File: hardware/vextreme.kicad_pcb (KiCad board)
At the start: 2 copper layers, 48 x 66.1 mm, 49 parts, among them CON1 vectrex-edge-connector, J1 USB_C_Receptacle_USB2.0, J2 Conn_01x06_Male, U1 LM1117-3.3, U2 STM32F411RCTx, U3 74HC32, U4 SN74LVC8T245DB, U5 W25Q128, Y1 8MHz

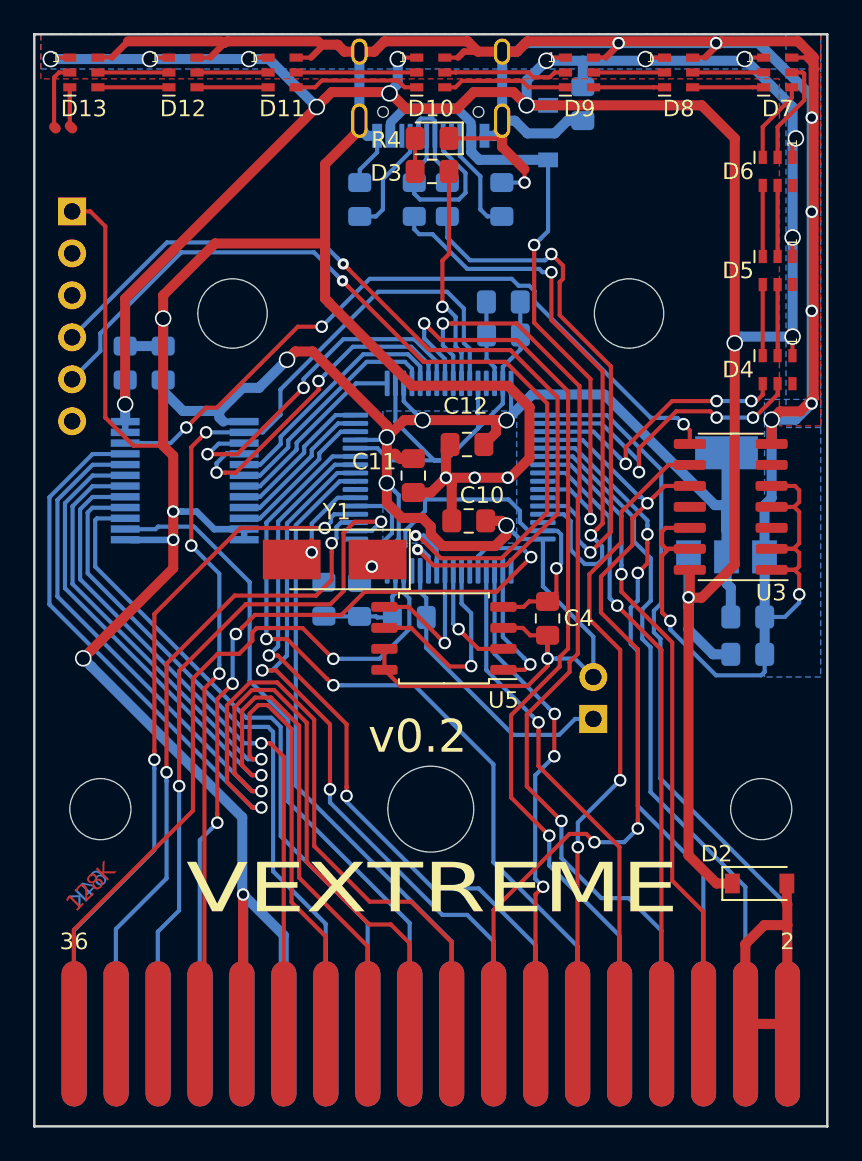
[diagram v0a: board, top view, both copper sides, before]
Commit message: v0.3 Hardware Changes
    - moved vextreme symbol library into libs/ folder
    - renaming 'veccart' to 'vextreme' for hardware files
    - Generate v0.3 gerbers, pdf and BOM
    - Finish routing v0.3 PCB
    - Fixes #21, added VEXTREME logo to PCB
    - Also moved most components to the bottom side and unrouted to prepare for single-sided conversion
    - Fixes #18, Add ESD protection to USB
    - Fixes #36, add test points for power rails.  Also add VEC-5V to PA10 to detect when Vectrex is on/off
    - Fixes #15, replace U3 with a single OR gate and add optional R7 to omit U3 completely
    - add SW1 for programming, add SW2 for STM32 reset
    - adds 3-pin header for LED output
    - Fixes #13, move the debugging/serial port connector so it does not interfere with enclosure bosses
    - Fixes #9, R4 & D3 reference designators are swapped
    - Fixes #12, reduce from 10 to 4 LEDs
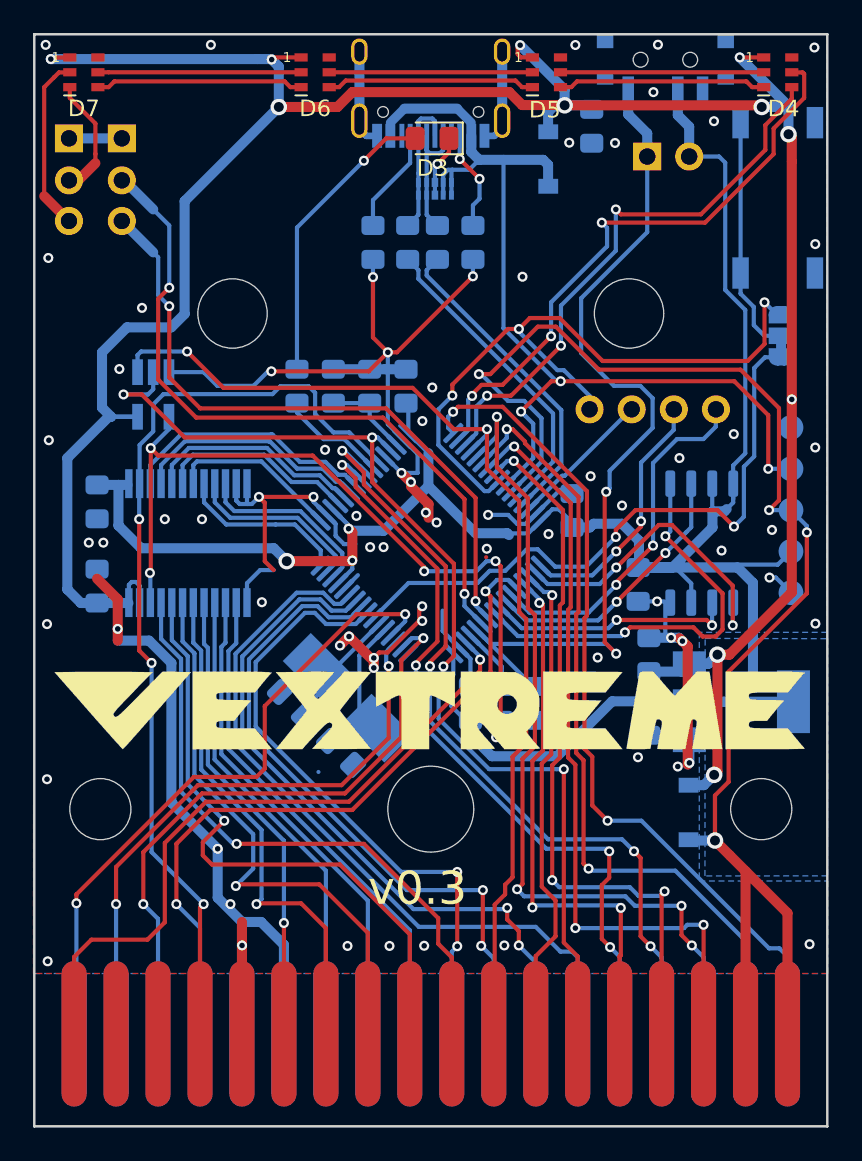
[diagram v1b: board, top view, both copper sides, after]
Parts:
- removed D10, D12, D8: APA102-2020, vextreme:LED-APA102-2020_6_REV_2
- removed the D4 at (162.7, 91.0)
- removed the D5 at (162.7, 85.0)
- removed the D6 at (162.7, 79.0)
- removed REF**: KiCad-Logo2_5mm_SilkScreen, Symbol:KiCad-Logo2_5mm_SilkScreen
- removed REF**: OSHW-Logo2_7.3x6mm_SilkScreen, Symbol:OSHW-Logo2_7.3x6mm_SilkScreen
- added G***: LOGO, vextreme:vextreme-logo, B.Cu at (141.7, 122.8)
- added G***: LOGO, vextreme:vextreme-logo, F.Cu at (141.7, 111.6)
- added J3: Conn_01x03_Male, Connector_PinHeader_2.54mm:PinHeader_1x03_P2.54mm_Vertical, B.Cu at (119.8, 77.0)
- added JP2: Jumper_3_Bridged12, vextreme:SolderJumper-3_P1.3mm_Bridged12_RoundedPad1.0x1.5mm_NumberLabels, B.Cu at (162.9, 89.0)
- added R7: 0, Resistor_SMD:R_0805_2012Metric_Pad1.15x1.40mm_HandSolder, B.Cu at (146.0, 111.2)
- added SP1: PA8, vextreme:SparePin_1x01_P2.54mm_Vertical, B.Cu at (151.3, 93.4)
- added SP2: PA13, vextreme:SparePin_1x01_P2.54mm_Vertical, B.Cu at (153.8, 93.4)
- added SP3: PA14, vextreme:SparePin_1x01_P2.54mm_Vertical, B.Cu at (156.4, 93.4)
- added SP4: PD2, vextreme:SparePin_1x01_P2.54mm_Vertical, B.Cu at (158.9, 93.4)
- added SW1: K3-1296S-E2, vextreme:SW_SPDT_K3-1296S-E2, B.Cu at (155.9, 72.6)
- added SW2: TS-1002S-11526C, vextreme:SW_Push_1P1T_NO_6x6mm_H11.5mm, B.Cu at (162.7, 80.6)
- added TP1: V5V, TestPoint:TestPoint_Pad_D1.5mm, B.Cu at (163.5, 99.5)
- added TP2: 5V, TestPoint:TestPoint_Pad_D1.5mm, B.Cu at (163.5, 94.5)
- added TP3: GND, TestPoint:TestPoint_Pad_D1.5mm, B.Cu at (163.5, 104.5)
- added TP4: U5V, TestPoint:TestPoint_Pad_D1.5mm, B.Cu at (163.5, 97.0)
- added TP5: 3V3, TestPoint:TestPoint_Pad_D1.5mm, B.Cu at (163.5, 102.0)
- added U6: TPD4E02B04DQA, vextreme:USON-10_2.5x1.0mm_P0.5mm_passthrough, B.Cu at (141.9, 80.0)
- C10, C11, C12, C4, D2, R4, U5, Y1: moved to B.Cu
- C13: value 47u -> 10u
- J2: value Conn_01x06_Male -> Conn_01x03_Male; footprint Connector_PinHeader_2.54mm:PinHeader_1x06_P2.54mm_Vertical -> Connector_PinHeader_2.54mm:PinHeader_1x03_P2.54mm_Vertical
- U3: value 74HC32 -> 74LVC1G32; footprint Package_SO:SOIC-14_3.9x8.7mm_P1.27mm -> vextreme:SOT-23-5_HandSoldering; moved to B.Cu
- moved U3 35.6 mm to (124.9, 92.5), turned to 270 degrees
- moved JP1 34.2 mm to (154.8, 78.1), turned to 270 degrees
- moved U5 16.6 mm to (158.1, 101.5), turned to 90 degrees
- moved R4 15.4 mm to (133.6, 92.0), turned to 270 degrees
- moved C5 13.6 mm to (121.5, 104.1)
- moved U1 12.0 mm to (160.5, 111.1), turned to 0 degrees
- moved C6 11.5 mm to (135.8, 92.0), turned to 90 degrees
- moved C10 11.0 mm to (144.1, 111.2), turned to 90 degrees
- moved C11 9.84 mm to (150.2, 99.5), turned to 90 degrees
- moved C8 9.36 mm to (136.3, 114.2), turned to 315 degrees
- moved C3 9.30 mm to (121.5, 99.0), turned to 270 degrees
- moved R3 9.13 mm to (147.9, 111.2), turned to 270 degrees
- moved C7 8.67 mm to (138.0, 92.0), turned to 90 degrees
- moved C2 8.57 mm to (154.9, 112.1), turned to 270 degrees
- moved Y1 8.41 mm to (136.7, 110.9), turned to 135 degrees
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- renumbered D7 to D4, D9 to D5, D11 to D6, D13 to D7
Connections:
- net USB-IN renamed USB-5V
- CON1 pad 2: C_VCC -> VEC-5V
- CON1 pad 4: C_VCC -> VEC-5V
- D2 pad 2: C_VCC -> VEC-5V
- D4 pad 2: Net-(D7-Pad2) (its old number) -> Net-(D4-Pad2)
- D4 pad 3: Net-(D7-Pad3) (its old number) -> Net-(D4-Pad3)
- D4 pad 4: Net-(D6-Pad3) -> SDAT
- D4 pad 5: Net-(D6-Pad2) -> SCLK
- D5 pad 2: Net-(D10-Pad5) -> Net-(D5-Pad2)
- D5 pad 3: Net-(D10-Pad4) -> Net-(D5-Pad3)
- D5 pad 4: SDAT_CONT -> Net-(D4-Pad3)
- D5 pad 5: SCLK_CONT -> Net-(D4-Pad2)
- D6 pad 2: Net-(D11-Pad2) -> Net-(D6-Pad2)
- D6 pad 3: Net-(D11-Pad3) -> Net-(D6-Pad3)
- D6 pad 4: Net-(D10-Pad3) -> Net-(D5-Pad3)
- D6 pad 5: Net-(D10-Pad2) -> Net-(D5-Pad2)
- D7 pad 4: Net-(D12-Pad3) -> Net-(D6-Pad3)
- D7 pad 5: Net-(D12-Pad2) -> Net-(D6-Pad2)
- J2 pad 2: Net-(J2-Pad2) -> RXD
- J2 pad 3: Net-(J2-Pad3) -> TXD
- U2 pad 29: Net-(U2-Pad29) -> V-OE
- U2 pad 41: Net-(U2-Pad41) -> PA8
- U2 pad 43: Net-(U2-Pad43) -> VEC-5V
- U2 pad 7: Net-(U2-Pad7) -> NRST
- U3 pad 1: GND -> V-CE
- U3 pad 2: GND -> V-OE
- U3 pad 3: Net-(U3-Pad3) -> GND
- U3 pad 4: GND -> Net-(R7-Pad1)
- U3 pad 5: GND -> +5V
- U4 pad 22: Net-(U3-Pad8) -> Net-(R7-Pad1)
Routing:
- net GND: track 421.8 -> 175.5 mm, vias 19 -> 74
- net VEC-5V: track 0.00 -> 88.3 mm, vias 0 -> 4
- net Net-(R7-Pad1): track 0.00 -> 48.2 mm, vias 0 -> 5
- net Net-(U3-Pad8): track 43.3 -> 0.00 mm, vias 3 -> 0
- net PA8: track 0.00 -> 41.9 mm, vias 0 -> 3
- net NRST: track 0.00 -> 38.1 mm, vias 0 -> 2
- net Net-(JP1-Pad1): track 17.5 -> 53.6 mm, vias 0 -> 2
- net +3V3: track 122.6 -> 157.5 mm, vias 7 -> 3
- net C_D7: track 67.9 -> 38.0 mm
- net V-OE: track 39.0 -> 65.2 mm, vias 2 -> 4
- net C_D6: track 61.6 -> 37.7 mm
- net Net-(SP4-Pad1): track 0.00 -> 21.6 mm, vias 0 -> 2
- net USB-5V: track 40.5 -> 61.4 mm, vias 2 -> 3
- net C_D5: track 58.9 -> 38.3 mm
- net C_VCC: track 18.9 -> 0.00 mm
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- added copper zone on B.Cu, net +3V3
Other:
- net class Large: via_drill 0.8 -> 0.6
- rule via_min_size: 0.6858 -> 0.6096
- board text added: "GND GND RXD DAT TXD CLK"
- board text added: "J2 J3"
- board text added: "v0.3"
- board text removed: "128K"
- board text removed: "64K"
- board text removed: "VEXTREME"
- board text removed: "v0.2"

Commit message: v0.4 Hardware Changes
- Increased length of SW2 to 12mm (TS-1002S-12026C)
- Changed SW1 to be the same as SW2
- Replaced J2 & J3 with a single 2x3 header that presses into place and holds
itself for soldering. Can use two separate 1x3 headers if desired.
- Replaced JP1 with a 1x2 header that presses into place for soldering.
- Added a micro 10-pin JTAG debugging header that doubles as USB Serial
adapter as well.
- Added a solderable jumper on V-NMI to be connected to one of PA8, which
also can be optionally connected to SW2.
- Added a diode for reverse polarity (cart upside down) on VEC_5V detect line. - Added a this side up label.
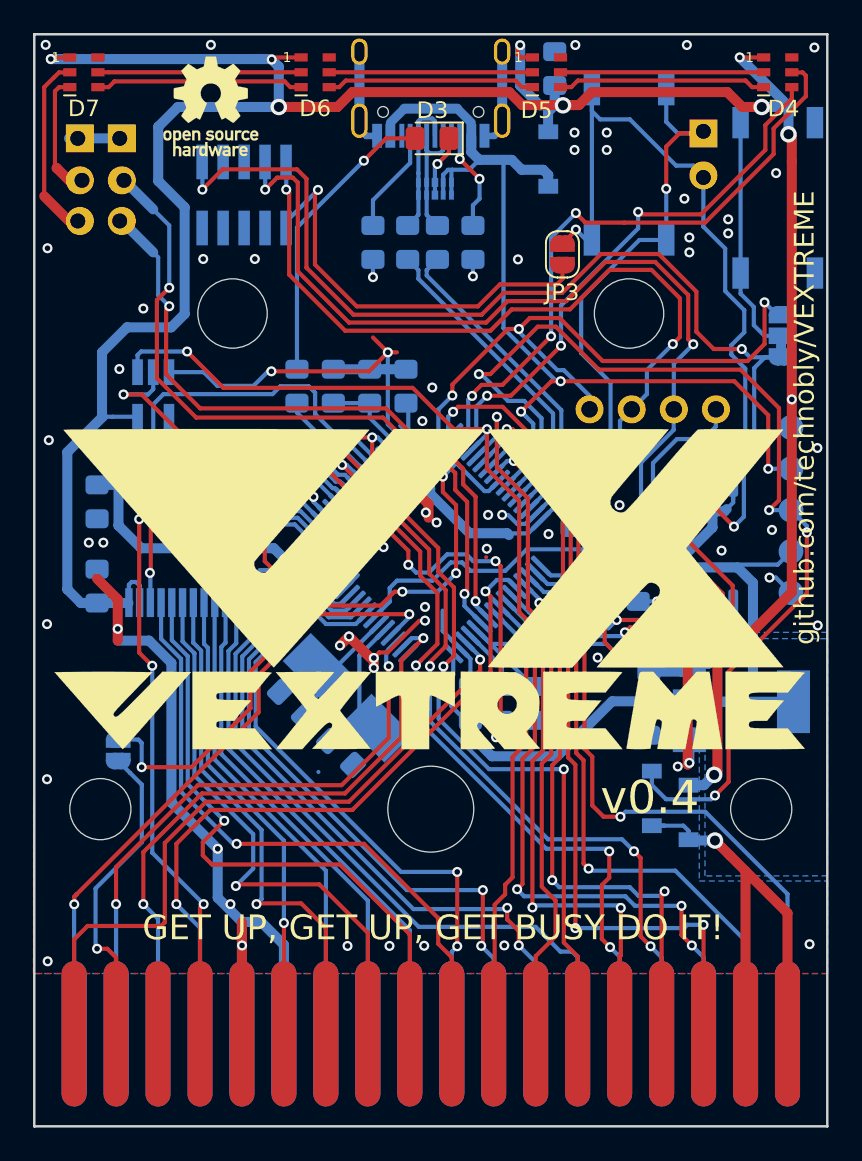
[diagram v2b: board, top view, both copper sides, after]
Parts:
- added D8: MBR0520, Diode_SMD:D_SOD-123, B.Cu at (155.1, 117.0)
- added G***: LOGO, vextreme:vx2-logo, F.Cu at (141.1, 101.6)
- added J4: FTSH-105-01-F-DV-K, vextreme:CONN5X2_1.27, B.Cu at (130.4, 80.4)
- added JP3: +3.3V Jumper, Jumper:SolderJumper-2_P1.3mm_Open_RoundedPad1.0x1.5mm, F.Cu at (149.7, 84.0)
- added JP4: V-NMI Jumper, Jumper:SolderJumper-2_P1.3mm_Open_RoundedPad1.0x1.5mm, B.Cu at (122.8, 114.0)
- added REF**: OSHW-Logo_5.7x6mm_SilkScreen, Symbol:OSHW-Logo_5.7x6mm_SilkScreen, F.Cu at (128.4, 75.1)
- J2, J3: footprint Connector_PinHeader_2.54mm:PinHeader_1x03_P2.54mm_Vertical -> vextreme:PinHeader_1x03_P2.54mm_Vertical_Odd_Even
- JP1: value Jumper_NO_Small -> Jumper; footprint Connector_PinHeader_2.54mm:PinHeader_1x02_P2.54mm_Vertical -> vextreme:PinHeader_1x02_P2.54mm_Vertical_Odd_Even
- SW1: value K3-1296S-E2 -> TS-1002S-12026C; footprint vextreme:SW_SPDT_K3-1296S-E2 -> vextreme:SW_Push_1P1T_NO_6x6mm_H12.0mm
- SW2: value TS-1002S-11526C -> TS-1002S-12026C; footprint vextreme:SW_Push_1P1T_NO_6x6mm_H11.5mm -> vextreme:SW_Push_1P1T_NO_6x6mm_H12.0mm
- moved SW1 6.42 mm to (153.7, 78.6), turned to 90 degrees
- moved C13 4.15 mm to (149.2, 72.8), turned to 90 degrees
- moved JP1 3.68 mm to (158.2, 76.7), turned to 180 degrees
- moved J3 0.66 mm to (120.5, 77.0)
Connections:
- net Net-(SP2-Pad1) renamed PA13
- net Net-(SP3-Pad1) renamed PA14
- CON1 pad 2: VEC-5V -> Net-(CON1-Pad2)
- CON1 pad 4: VEC-5V -> Net-(CON1-Pad2)
- D2 pad 2: VEC-5V -> Net-(CON1-Pad2)
- SP1 pad 1: PA8 -> NMI
- U2 pad 41: PA8 -> NMI
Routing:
- net NMI: track 0.00 -> 77.4 mm, vias 0 -> 7
- net NRST: track 38.1 -> 87.7 mm, vias 2 -> 4
- net PA14: track 15.4 -> 59.7 mm, vias 2 -> 4
- net PA13: track 8.62 -> 52.3 mm, vias 0 -> 2
- net PA8: track 41.9 -> 0.00 mm, vias 3 -> 0
- net Net-(CON1-Pad2): track 0.00 -> 30.0 mm, vias 0 -> 1
- net Net-(J4-Pad1): track 0.00 -> 25.2 mm, vias 0 -> 1
- net VEC-5V: track 88.3 -> 64.3 mm
- net V-NMI: track 0.00 -> 23.5 mm, vias 0 -> 1
- net +3V3: track 157.5 -> 172.6 mm, vias 3 -> 4
- net GND: track 175.5 -> 163.4 mm, vias 74 -> 82
- net +5V: track 166.1 -> 169.5 mm
- net V-HALT: track 51.4 -> 53.9 mm
- net SCLK: track 36.2 -> 37.8 mm
- net Net-(JP1-Pad1): track 53.6 -> 55.1 mm, vias 2 -> 3
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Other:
- board text added: "GET DOWN, GET DOWN!"
- board text added: "GET UP, GET UP, GET BUSY DO IT!"
- board text added: "github.com/technobly/VEXTREME"
- board text added: "v0.4"
- board text removed: "J2 J3"
- board text removed: "v0.3"

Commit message: v0.5 Hardware Changes
- Added a location for a Wi-Fi module
- Changed J2 to support +5V for the Wi-Fi module
- Changed the artwork a bit and side up/down text
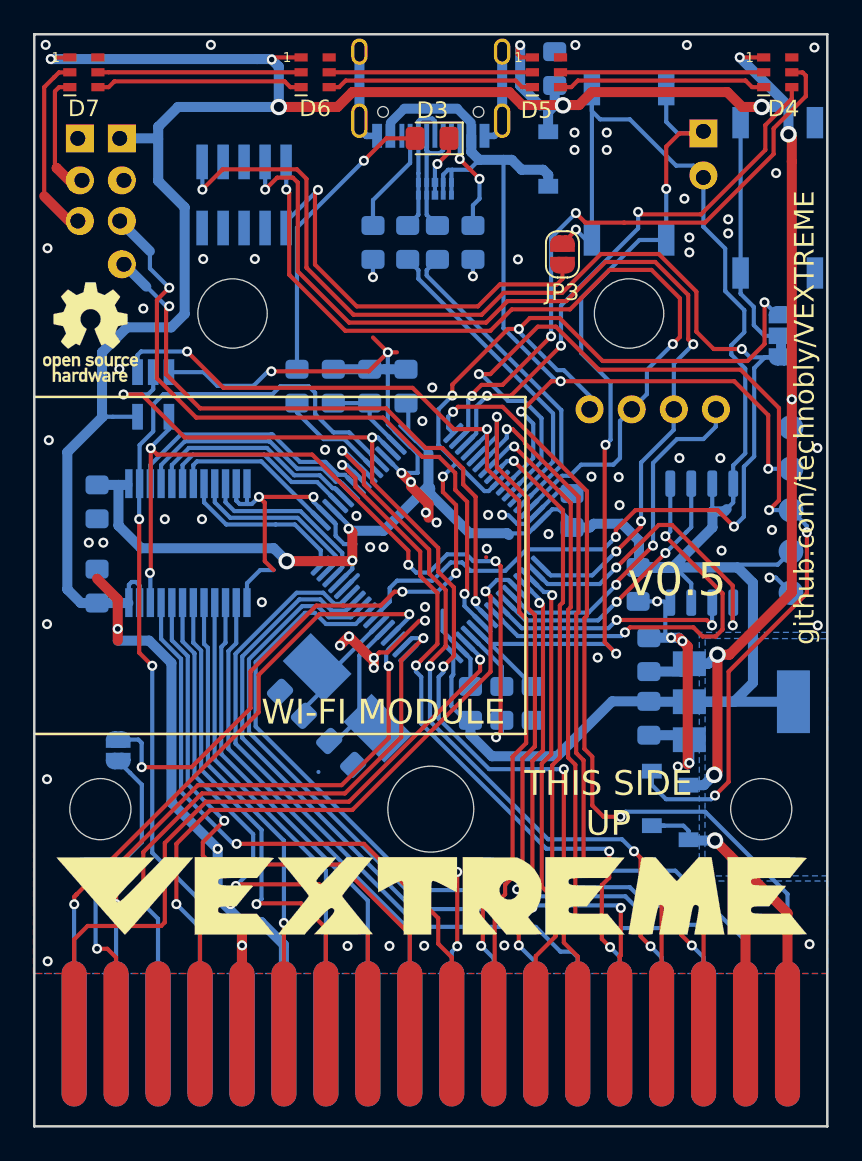
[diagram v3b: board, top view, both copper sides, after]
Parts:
- removed the G*** at (141.1, 101.6)
- J2: value Conn_01x03_Male -> Conn_01x04_Male; footprint vextreme:PinHeader_1x03_P2.54mm_Vertical_Odd_Even -> vextreme:PinHeader_1x04_P2.54mm_Vertical_Odd_Even
- moved REF** 15.5 mm to (121.1, 88.7)
- moved G*** 11.2 mm to (141.8, 122.8)
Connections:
- J2 pad 1: GND -> +5V
- J2 pad 2: RXD -> GND
- J2 pad 3: TXD -> RXD
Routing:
- net GND: track 163.4 -> 160.3 mm
- net TXD: track 40.6 -> 38.0 mm
- net RXD: track 44.0 -> 41.5 mm
- net +5V: track 169.5 -> 171.8 mm
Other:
- board text added: "+5V GND RX TX"
- board text added: "GND DAT CLK"
- board text added: "THIS SIDE DOWN"
- board text added: "THIS SIDE UP"
- board text added: "WI-FI MODULE"
- board text added: "v0.5"
- board text removed: "GET DOWN, GET DOWN!"
- board text removed: "GET UP, GET UP, GET BUSY DO IT!"
- board text removed: "GND GND RXD DAT TXD CLK"
- board text removed: "v0.4"

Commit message: v1.0 Hardware Changes
- Bumped the version number
- I think that's all I did?? :D
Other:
- board text added: "v1.0"
- board text removed: "v0.5"
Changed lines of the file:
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@@
   (title_block
     (title "VEXTREME Vectrex Multicart")
-    (date 2021-05-15)
-    (rev v0.5)
+    (date 2021-06-19)
+    (rev v1.0)
   )
   (layers
@@
       (effects (font (size 1 1) (thickness 0.15)) (justify mirror))
     )
-    (fp_text user %R (at 0 -2.54 90) (layer B.Fab) hide
-      (effects (font (size 1 1) (thickness 0.15)) (justify mirror))
-    )
     (fp_line (start -0.635 1.27) (end 1.27 1.27) (layer B.Fab) (width 0.1))
     (fp_line (start 1.27 1.27) (end 1.275 -8.725) (layer B.Fab) (width 0.1))
@@
     (fp_line (start 1.8 -9.175) (end 1.8 1.8) (layer B.CrtYd) (width 0.05))
     (fp_line (start 1.8 1.8) (end -1.8 1.8) (layer B.CrtYd) (width 0.05))
+    (fp_text user %R (at 0 -2.54 90) (layer B.Fab) hide
+      (effects (font (size 1 1) (thickness 0.15)) (justify mirror))
+    )
     (pad 4 thru_hole oval (at -0.127 -7.62 180) (size 1.7 1.7) (drill 0.9144 (offset 0.127 0)) (layers *.Cu *.Mask)
       (net 51 TXD))
@@
   (gr_line (start 153.7 87.6) (end 153.7 117.6) (layer F.Fab) (width 0.15))
   (gr_line (start 121.7 117.6) (end 161.7 117.6) (layer F.Fab) (width 0.15))
-  (gr_text v0.5 (at 156.6 103.725) (layer F.SilkS)
+  (gr_text v1.0 (at 156.6 103.725) (layer F.SilkS)
     (effects (font (size 2 2) (thickness 0.3)))
   )
@@
   (via (at 131.05 84.3) (size 0.6096) (drill 0.3302) (layers F.Cu B.Cu) (net 2))
   (via (at 146.02 99.79) (size 0.6096) (drill 0.3302) (layers F.Cu B.Cu) (net 2))
+  (segment (start 123.14 79.54) (end 123 79.54) (width 0.6096) (layer B.Cu) (net 2))
   (via (at 143.05 93.549994) (size 0.6096) (drill 0.3302) (layers F.Cu B.Cu) (net 3))
   (segment (start 142.75 93.849994) (end 143.05 93.549994) (width 0.254) (layer B.Cu) (net 3))
@@
   (segment (start 144.41 98.69) (end 143.66 97.94) (width 0.254) (layer F.Cu) (net 51))
   (segment (start 144.41 105.009998) (end 144.41 98.69) (width 0.254) (layer F.Cu) (net 51))
-  (segment (start 123.14 79.54) (end 123 79.54) (width 0.6096) (layer B.Cu) (net 2))
   (segment (start 124.482 85.975) (end 123.127 84.62) (width 0.6096) (layer B.Cu) (net 51))
   (segment (start 124.5 85.975) (end 124.482 85.975) (width 0.254) (layer B.Cu) (net 51))
